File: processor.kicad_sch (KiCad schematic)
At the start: 80 parts, among them J1 Conn_01x40, Q1 2N3904, Q2 2N3904, Q3 2N3904, Q4 2N3904, Q5 2N3904, SW1 RESET, U1 68000, U2 27C010, U3 27C010, U4 74HC74, U5 LM555xM, U6 74LS06, Y1 4.433618MHz, Y2 30.084988MHz

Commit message: motherboard: Added the BLiTTER to the schematic and tidied up a pile
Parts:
- added R100, R101, R99: 10k, rhais_rcl:R0603, symbol Device:R_Small
- added U39: STB, Package_LCC:PLCC-68_SMD-Socket, symbol dragonSTe:STB
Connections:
- net +5V: now also R100.1, R101.1, R99.1, U39.1 (VCC), U39.33 (VCC)
- net CLK8: now also U39.34 (CLK)
- net GND: now also U39.35 (GND), U39.5 (GND)
- net SysBus.A1: now also U39.47 (A1)
- net SysBus.A10: now also U39.56 (A10)
- net SysBus.A11: now also U39.57 (A11)
- net SysBus.A12: now also U39.58 (A12)
- net SysBus.A13: now also U39.59 (A13)
- net SysBus.A14: now also U39.61 (A14)
- net SysBus.A15: now also U39.62 (A15)
- net SysBus.A16: now also U39.63 (A16)
- net SysBus.A17: now also U39.64 (A17)
- net SysBus.A18: now also U39.65 (A18)
- net SysBus.A19: now also U39.66 (A19)
- net SysBus.A2: now also U39.48 (A2)
- net SysBus.A20: now also U39.67 (A20)
- net SysBus.A21: now also U39.2 (A21)
- net SysBus.A22: now also U39.3 (A22)
- net SysBus.A23: now also U39.4 (A23)
- net SysBus.A3: now also U39.49 (A3)
- net SysBus.A4: now also U39.50 (A4)
- net SysBus.A5: now also U39.51 (A5)
- net SysBus.A6: now also U39.52 (A6)
- net SysBus.A7: now also U39.53 (A7)
- net SysBus.A8: now also U39.54 (A8)
- net SysBus.A9: now also U39.55 (A9)
- net SysBus.D0: now also U39.21 (D0)
- net SysBus.D1: now also U39.20 (D1)
- net SysBus.D10: now also U39.11 (D10)
- net SysBus.D11: now also U39.10 (D11)
- net SysBus.D12: now also U39.9 (D12)
- net SysBus.D13: now also U39.8 (D13)
- net SysBus.D14: now also U39.7 (D14)
- net SysBus.D15: now also U39.6 (D15)
- net SysBus.D2: now also U39.19 (D2)
- net SysBus.D3: now also U39.18 (D3)
- net SysBus.D4: now also U39.17 (D4)
- net SysBus.D5: now also U39.16 (D5)
- net SysBus.D6: now also U39.15 (D6)
- net SysBus.D7: now also U39.14 (D7)
- net SysBus.D8: now also U39.13 (D8)
- net SysBus.D9: now also U39.12 (D9)
- net SysBus.R/~{W}: now also U39.26 (R/~{W})
- net SysBus.~{AS}: now also U39.23 (~{AS})
- net SysBus.~{DTACK}: now also U39.27 (~{DTACK})
- net SysBus.~{LDS}: now also U39.25 (~{LDS})
- net SysBus.~{UDS}: now also U39.24 (~{UDS})
- net ~{BGACK}: now also U39.29 (~{BGACK})
- net ~{BR}: now also U39.30 (~{BR})
- net ~{BUS_ERR}: now also U39.38 (~{BERR})
- net ~{RESET}: now also U39.36 (~{RESET})
- net ~{CPU_BG}: now reaches U1.11 (BG)
- net ~{CPU_BG}: now also U39.28 (~{BGI})
- net FC2: now reaches U1.26 (FC2)
- net FC2: now also R101.2, U39.43 (FC2)
- net FC1: now reaches U1.27 (FC1)
- net FC1: now also R100.2, U39.44 (FC1)
- net FC0: now reaches U1.28 (FC0)
- net FC0: now also R99.2, U39.45 (FC0)
- new net ~{BGK}: U39.40 (~{BGKI})
- new net ~{BLT_BG}: U39.37 (~{BGO})
- new net ~{BLT_INT}: U39.41 (~{INT})

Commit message: motherboard: Worked on fleshing out more of the top-level schematic, filling in more of the connections that need to be made between blocks
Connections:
- net ~{IPL2}: now reaches U1.23 (IPL2)
- net ~{IPL1}: now reaches U1.24 (IPL1)
- net ~{IPL0}: now reaches U1.25 (IPL0)

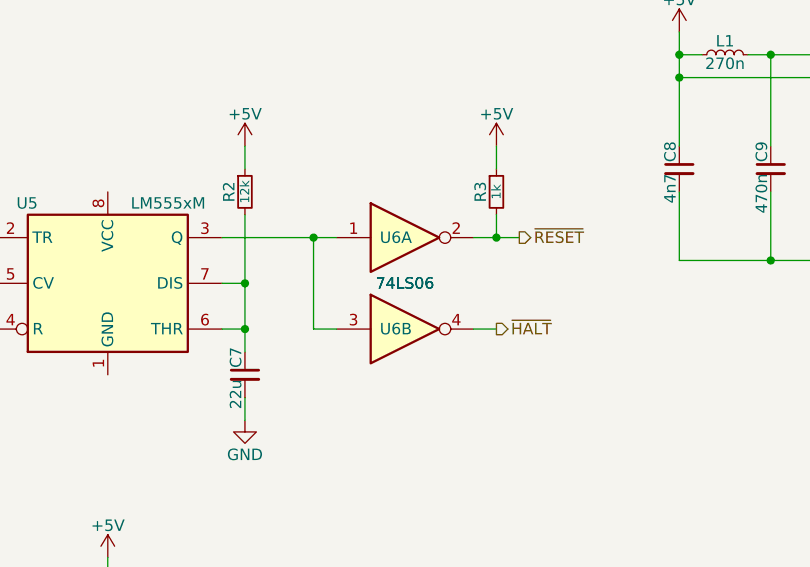
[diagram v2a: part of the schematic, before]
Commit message: motherboard: More signal routing, and starting in on the BoM
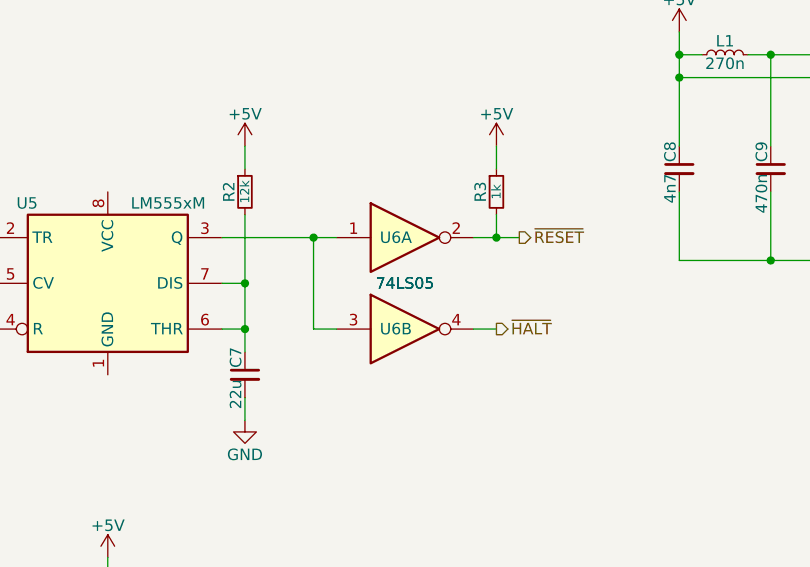
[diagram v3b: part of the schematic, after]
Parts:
- U6: value 74LS06 -> 74LS05; footprint (none) -> Package_SO:SO-14_3.9x8.65mm_P1.27mm; MFR (none) -> TI; MPN (none) -> SN74HC05DR; OC_FARNELL (none) -> 3120437

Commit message: motherboard: Begun routing the internal floppy disk interface
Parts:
- U5: footprint Package_SO:SOIC-8_3.9x4.9mm_P1.27mm -> rhais_package-smd:SO-8_3.9x4.9mm_P1.27mm
- U6: footprint Package_SO:SO-14_3.9x8.65mm_P1.27mm -> rhais_package-smd:SO-14_3.9x8.65mm_P1.27mm
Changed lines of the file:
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@@
 			)
 		)
-		(property "Footprint" "Package_SO:SOIC-8_3.9x4.9mm_P1.27mm"
+		(property "Footprint" "rhais_package-smd:SO-8_3.9x4.9mm_P1.27mm"
 			(at 110.49 73.66 0)
 			(effects
@@
 			)
 		)
-		(property "Footprint" "Package_SO:SO-14_3.9x8.65mm_P1.27mm"
+		(property "Footprint" "rhais_package-smd:SO-14_3.9x8.65mm_P1.27mm"
 			(at 121.92 58.42 0)
 			(effects
@@
 			)
 		)
-		(property "Footprint" "Package_SO:SO-14_3.9x8.65mm_P1.27mm"
+		(property "Footprint" "rhais_package-smd:SO-14_3.9x8.65mm_P1.27mm"
 			(at 121.92 68.58 0)
 			(effects

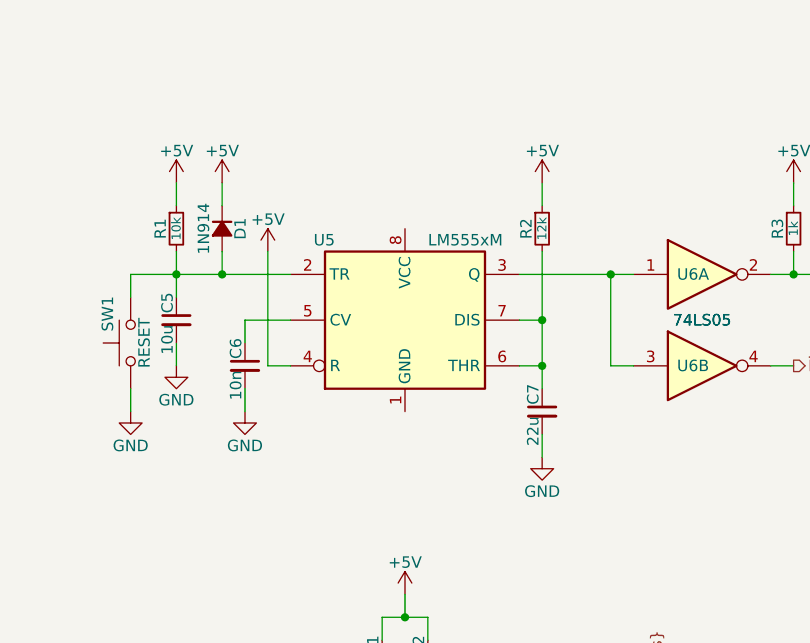
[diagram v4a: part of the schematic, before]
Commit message: motherboard: Routed one of the parallel interfaces and the ROMs
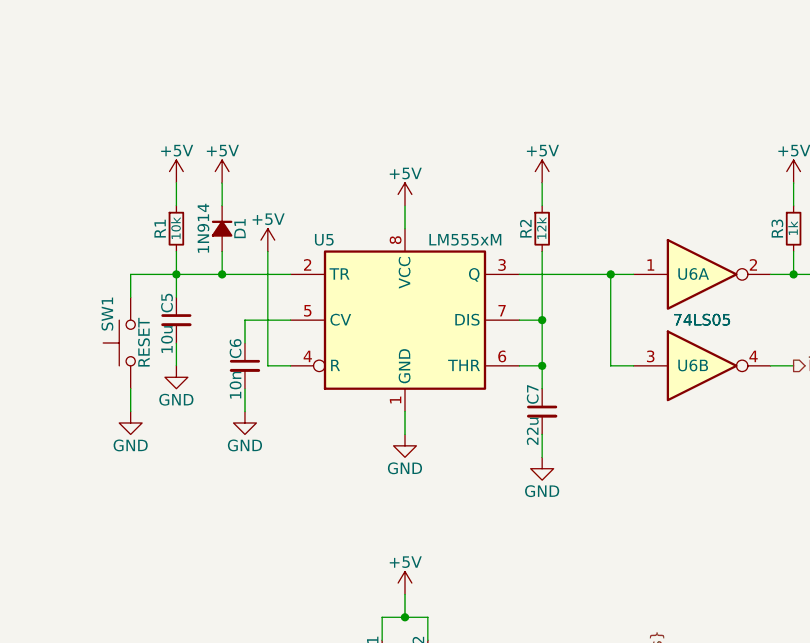
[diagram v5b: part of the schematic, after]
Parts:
- Q1, Q2, Q3, Q4, Q5: footprint (none) -> rhais_package-smd:SOT-23
- U2, U3: footprint (none) -> rhais_package-dip:DIP-32_W15.24mm_Socket
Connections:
- net +5V: now also U5.8 (VCC)
- net GND: now also U5.1 (GND)
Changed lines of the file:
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@@
 		)
 	)
+	(wire
+		(pts
+			(xy 88.9 73.66) (xy 88.9 76.2)
+		)
+		(stroke
+			(width 0)
+			(type default)
+		)
+	)
 	(bus
 		(pts
@@
 		)
 	)
+	(wire
+		(pts
+			(xy 88.9 50.8) (xy 88.9 53.34)
+		)
+		(stroke
+			(width 0)
+			(type default)
+		)
+	)
 	(bus
 		(pts
@@
 			)
 		)
-		(property "Footprint" ""
+		(property "Footprint" "rhais_package-dip:DIP-32_W15.24mm_Socket"
 			(at 241.3 203.2 0)
 			(effects
@@
 			)
 		)
-		(property "Footprint" ""
+		(property "Footprint" "rhais_package-smd:SOT-23"
 			(at 203.2 45.72 0)
 			(effects
@@
 			)
 		)
-		(property "Footprint" ""
+		(property "Footprint" "rhais_package-smd:SOT-23"
 			(at 289.56 50.8 0)
 			(effects
@@
 			)
 		)
-		(property "Footprint" ""
+		(property "Footprint" "rhais_package-dip:DIP-32_W15.24mm_Socket"
 			(at 190.5 203.2 0)
 			(effects
@@
 			)
 		)
-		(property "Footprint" ""
+		(property "Footprint" "rhais_package-smd:SOT-23"
 			(at 347.98 45.72 0)
 			(effects
@@
 			)
 		)
-		(property "Footprint" ""
+		(property "Footprint" "rhais_package-smd:SOT-23"
 			(at 383.54 48.26 0)
 			(effects
@@
 	)
 	(symbol
+		(lib_id "power:+5V")
+		(at 88.9 50.8 0)
+		(unit 1)
+		(exclude_from_sim no)
+		(in_bom yes)
+		(on_board yes)
+		(dnp no)
+		(property "Reference" "#PWR0273"
+			(at 88.9 54.61 0)
+			(effects
+				(font
+					(size 1.27 1.27)
+				)
+				(hide yes)
+			)
+		)
+		(property "Value" "+5V"
+			(at 88.9 47.244 0)
+			(effects
+				(font
+					(size 1.27 1.27)
+				)
+			)
+		)
+		(property "Footprint" ""
+			(at 88.9 50.8 0)
+			(effects
+				(font
+					(size 1.27 1.27)
+				)
+				(hide yes)
+			)
+		)
+		(property "Datasheet" ""
+			(at 88.9 50.8 0)
+			(effects
+				(font
+					(size 1.27 1.27)
+				)
+				(hide yes)
+			)
+		)
+		(property "Description" "Power symbol creates a global label with name \"+5V\""
+			(at 88.9 50.8 0)
+			(effects
+				(font
+					(size 1.27 1.27)
+				)
+				(hide yes)
+			)
+		)
+		(pin "1"
+		)
+		(instances
+			(project "dragonSTe"
+				(path "/6cc81c6b-09a2-4492-8ca2-d80a5c796e77/ee1ee771-c1d0-461a-948a-297a1c42437c"
+					(reference "#PWR0273")
+					(unit 1)
+				)
+			)
+		)
+	)
+	(symbol
 		(lib_id "Device:C_Small")
 		(at 269.24 45.72 0)
@@
 			)
 		)
-		(property "Footprint" ""
+		(property "Footprint" "rhais_package-smd:SOT-23"
 			(at 236.22 48.26 0)
 			(effects
@@
 					(unit 1)
 				)
+			)
+		)
+	)
+	(symbol
+		(lib_id "power:GND")
+		(at 88.9 76.2 0)
+		(unit 1)
+		(exclude_from_sim no)
+		(in_bom yes)
+		(on_board yes)
+		(dnp no)
+		(property "Reference" "#PWR0262"
+			(at 88.9 82.55 0)
+			(effects
+				(font
+					(size 1.27 1.27)
+				)
+				(hide yes)
+			)
+		)
+		(property "Value" "GND"
+			(at 88.9 80.01 0)
+			(effects
+				(font
+					(size 1.27 1.27)
+				)
+			)
+		)
+		(property "Footprint" ""
+			(at 88.9 76.2 0)
+			(effects
+				(font
+					(size 1.27 1.27)
+				)
+				(hide yes)
+			)
+		)
+		(property "Datasheet" ""
+			(at 88.9 76.2 0)
+			(effects
+				(font
+					(size 1.27 1.27)
+				)
+				(hide yes)
+			)
+		)
+		(property "Description" "Power symbol creates a global label with name \"GND\" , ground"
+			(at 88.9 76.2 0)
+			(effects
+				(font
+					(size 1.27 1.27)
+				)
+				(hide yes)
+			)
+		)
+		(pin "1"
+		)
+		(instances
+			(project "dragonSTe"
+				(path "/6cc81c6b-09a2-4492-8ca2-d80a5c796e77/ee1ee771-c1d0-461a-948a-297a1c42437c"
+					(reference "#PWR0262")
+					(unit 1)
+				)

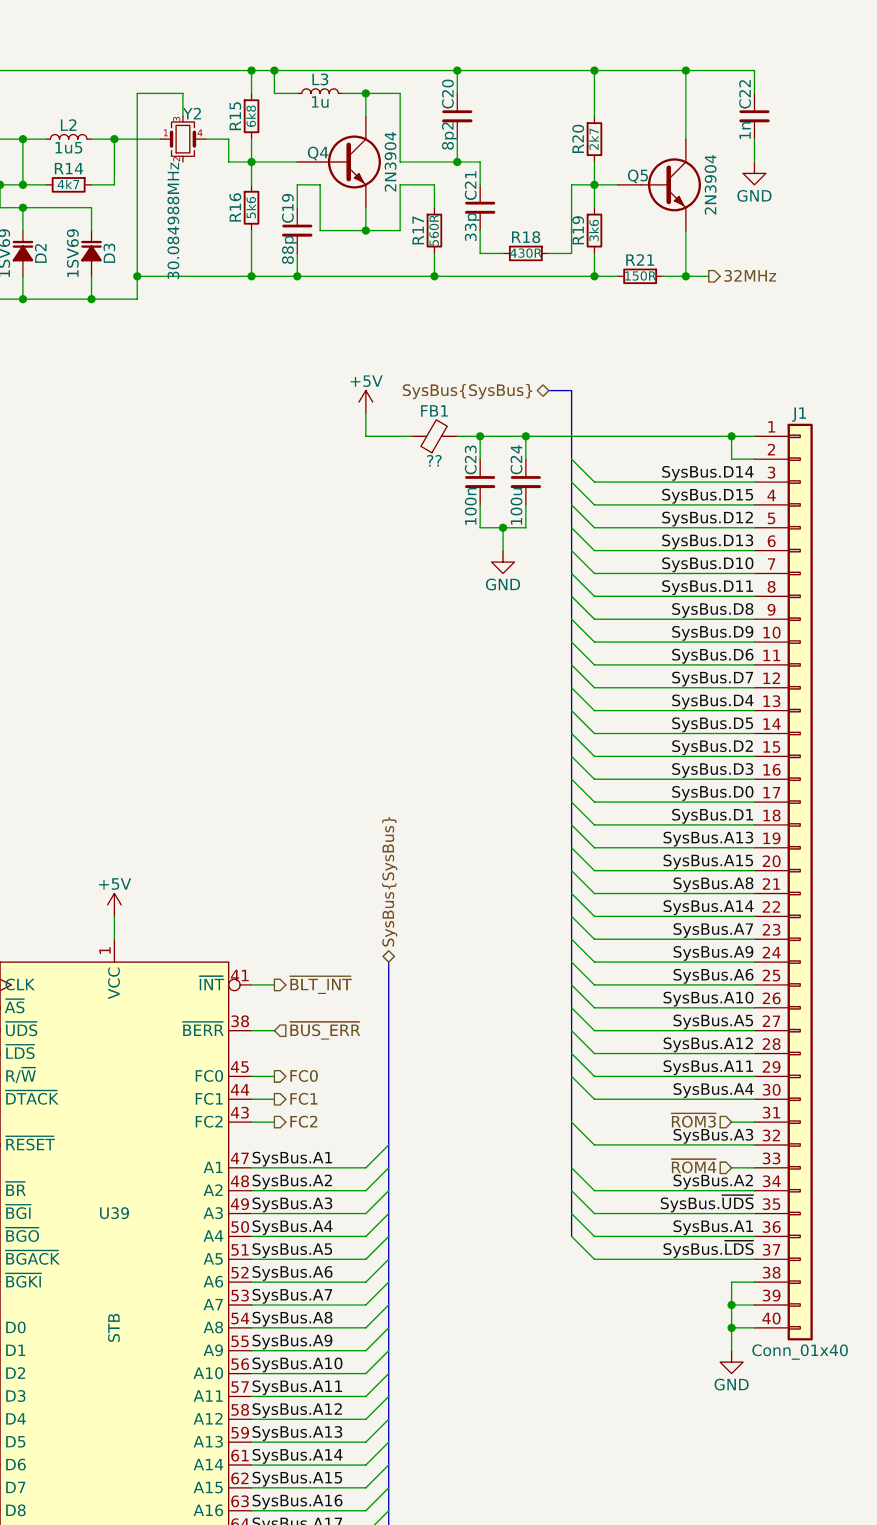
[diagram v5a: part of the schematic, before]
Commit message: motherboard: Fixed the floppy power connector and defined the board parameters for manufacture
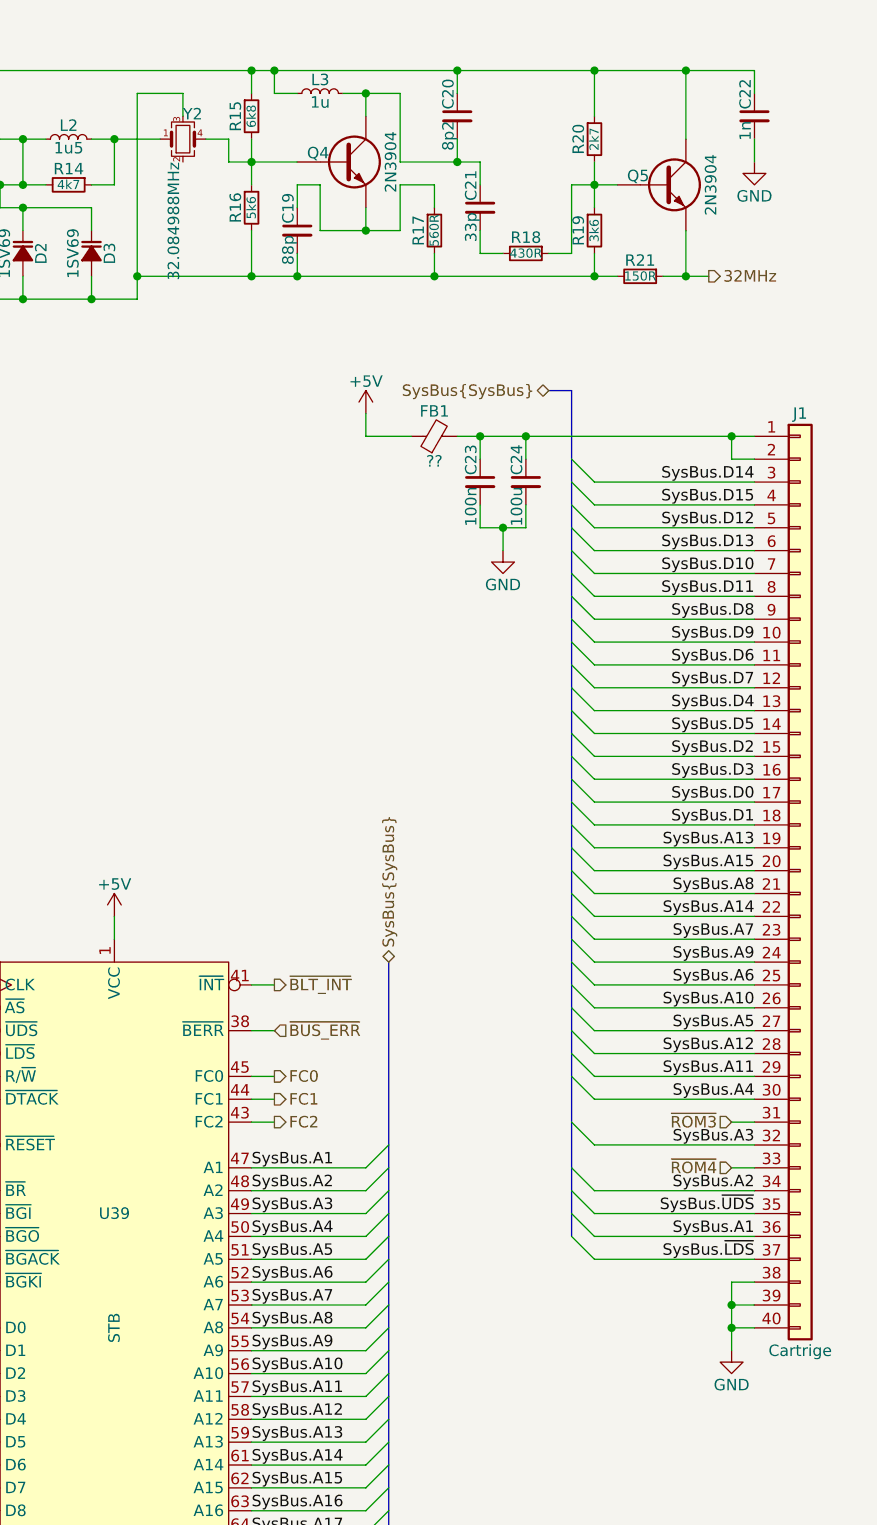
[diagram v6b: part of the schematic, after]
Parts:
- J1: value Conn_01x40 -> Cartrige
- Y2: value 30.084988MHz -> 32.084988MHz
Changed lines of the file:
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@@
 			)
 		)
-		(property "Value" "Conn_01x40"
+		(property "Value" "Cartrige"
 			(at 393.7 180.34 0)
 			(effects
@@
 			)
 		)
-		(property "Value" "30.084988MHz"
+		(property "Value" "32.084988MHz"
 			(at 324.104 48.26 90)
 			(effects
